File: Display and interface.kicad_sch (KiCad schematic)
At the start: 0 parts

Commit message: расставлены основные блоки и компоненты, подобраны компоненты интерфейса и питания
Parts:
- added HG1: ~, IPS_ST7735_0_96:ST7735 0.96, symbol ST7735 0_96:ST7735_0.96
- added J2: Micro_SD_Card_Det2, Connector_Card:microSD_HC_Hirose_DM3AT-SF-PEJM5, symbol Connector:Micro_SD_Card_Det2
- added SW1, SW2, SW3, SW4: SW_Push, Button_Switch_SMD:SW_Push_1P1T_NO_Vertical_Wuerth_434133025816, symbol Switch:SW_Push
- added U4: SPI-EEPROM, Package_SO:SOIC-8_3.9x4.9mm_P1.27mm, symbol Memory_EEPROM:M95256-WMN6P

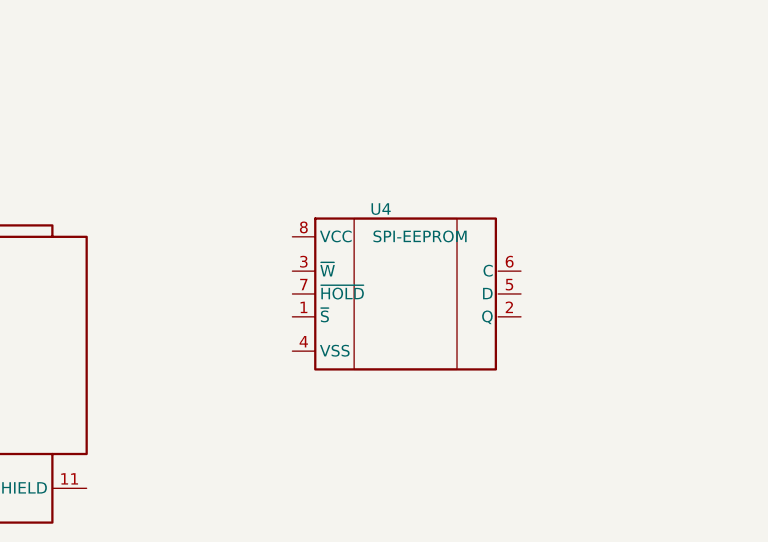
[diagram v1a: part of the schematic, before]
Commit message: Внесены распиновки интерфейсного модуля и модуля GPIO + конденсаторы по питанию 2/7 референсной схемы
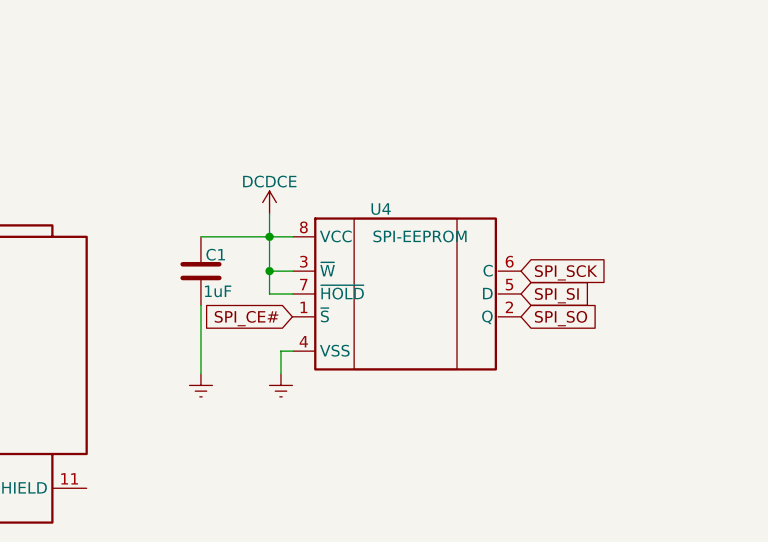
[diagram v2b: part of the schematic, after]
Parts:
- added C1: 1uF, Capacitor_SMD:C_0402_1005Metric, symbol Device:C
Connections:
- net SPI_CE#: now reaches U4.1 (~{S})
- net SPI_SO: now reaches U4.2 (Q)
- net DCDCE: now reaches U4.3 (~{W})
- net DCDCE: now also U4.7 (~{HOLD}), U4.8 (VCC), C1.1
- net Earth: now reaches U4.4 (VSS)
- net Earth: now also C1.2
- net SPI_SI: now reaches U4.5 (D)
- net SPI_SCK: now reaches U4.6 (C)

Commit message: Обновлена структура, закончен интерфейс, HDMI Завершено проектирование линий питания и подтяжек для интерфейсов
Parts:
- removed C1: 1uF, Capacitor_SMD:C_0402_1005Metric, symbol Device:C
- removed HG1: ~, IPS_ST7735_0_96:ST7735 0.96, symbol ST7735 0_96:ST7735_0.96
- removed J2: Micro_SD_Card_Det2, Connector_Card:microSD_HC_Hirose_DM3AT-SF-PEJM5, symbol Connector:Micro_SD_Card_Det2
- removed SW1, SW2, SW3, SW4: SW_Push, Button_Switch_SMD:SW_Push_1P1T_NO_Vertical_Wuerth_434133025816, symbol Switch:SW_Push
- removed U4: SPI-EEPROM, Package_SO:SOIC-8_3.9x4.9mm_P1.27mm, symbol Memory_EEPROM:M95256-WMN6P
